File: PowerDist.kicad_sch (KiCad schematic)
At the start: 19 parts, among them U1 TPS2121RUXR

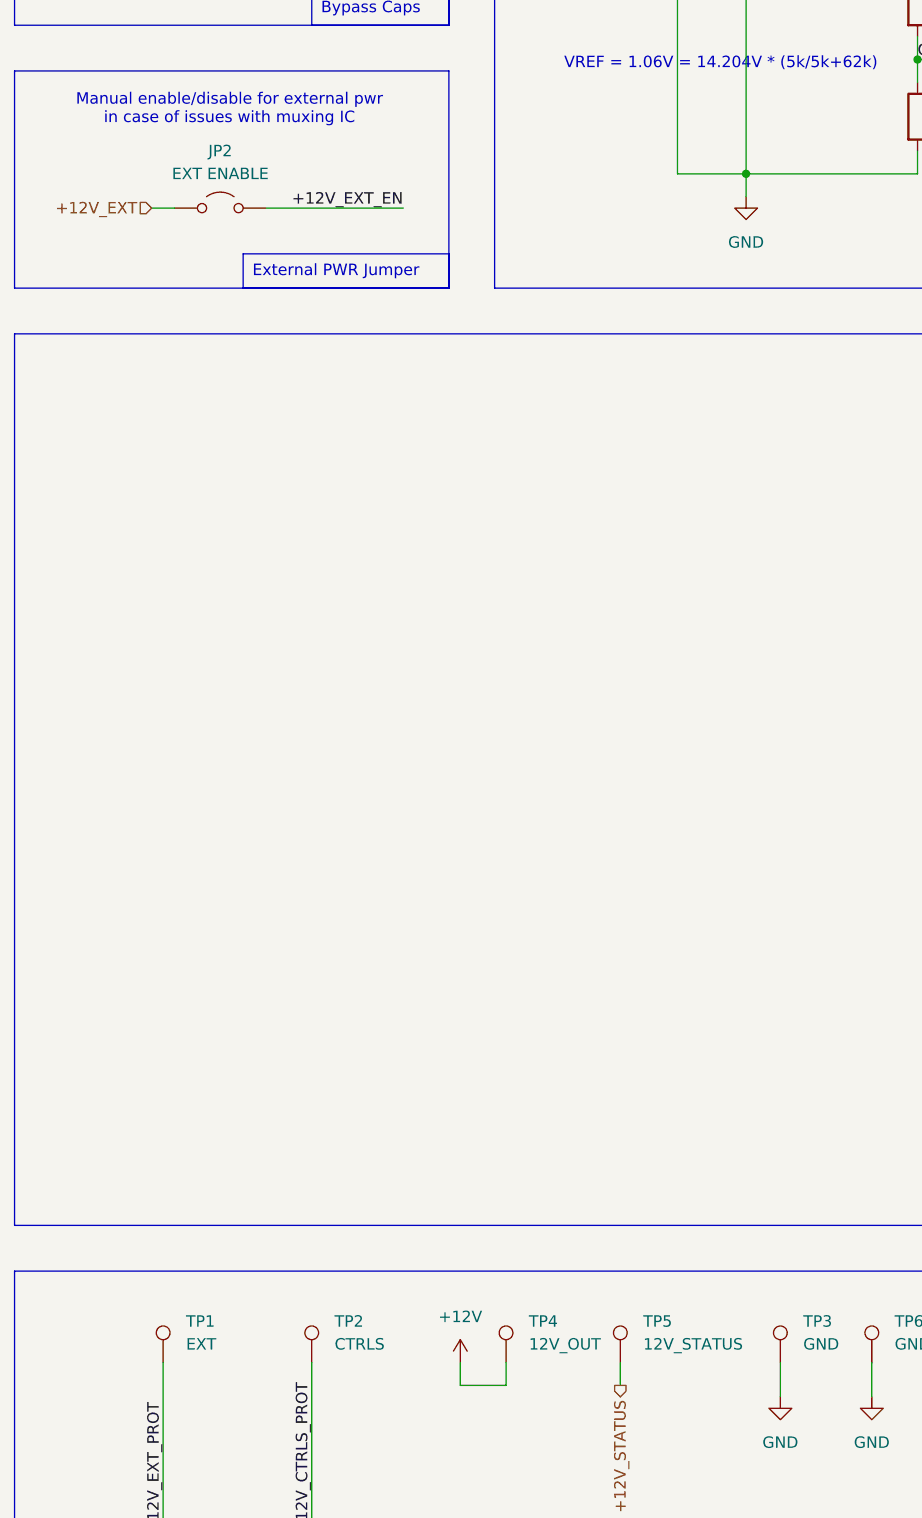
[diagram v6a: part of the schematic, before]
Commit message: flip connectors so clip faces inside
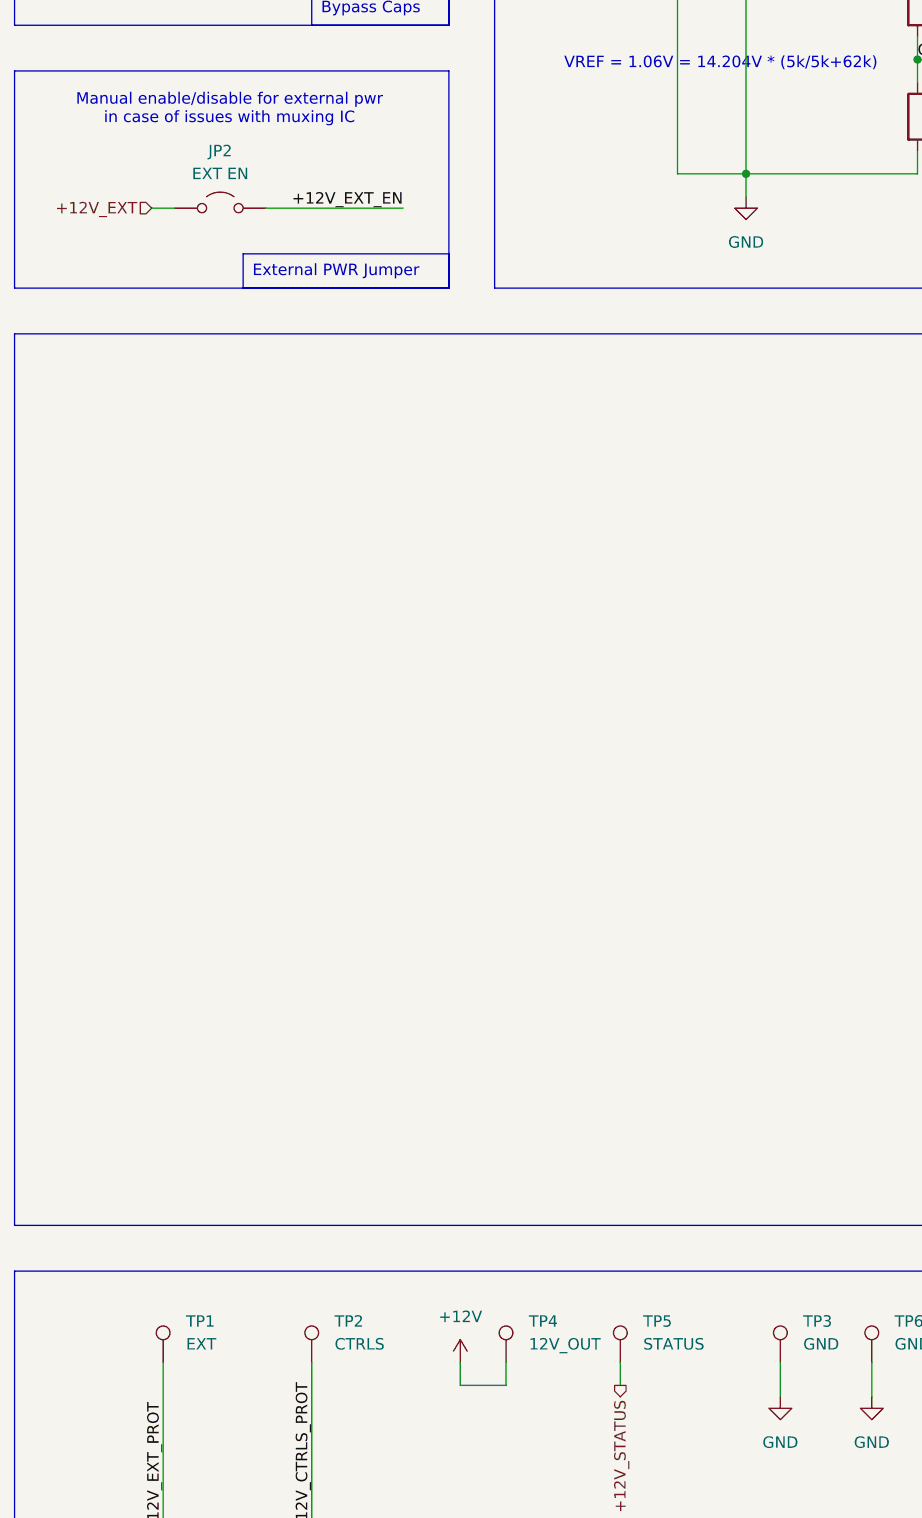
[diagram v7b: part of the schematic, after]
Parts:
- JP2: value EXT ENABLE -> EXT EN
- TP5: value 12V_STATUS -> STATUS
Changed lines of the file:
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@@
 			)
 		)
-		(property "Value" "12V_STATUS"
+		(property "Value" "STATUS"
 			(at 88.9 237.9979 0)
 			(effects
@@
 			)
 		)
-		(property "Value" "EXT ENABLE"
+		(property "Value" "EXT EN"
 			(at 41.91 107.95 0)
 			(effects

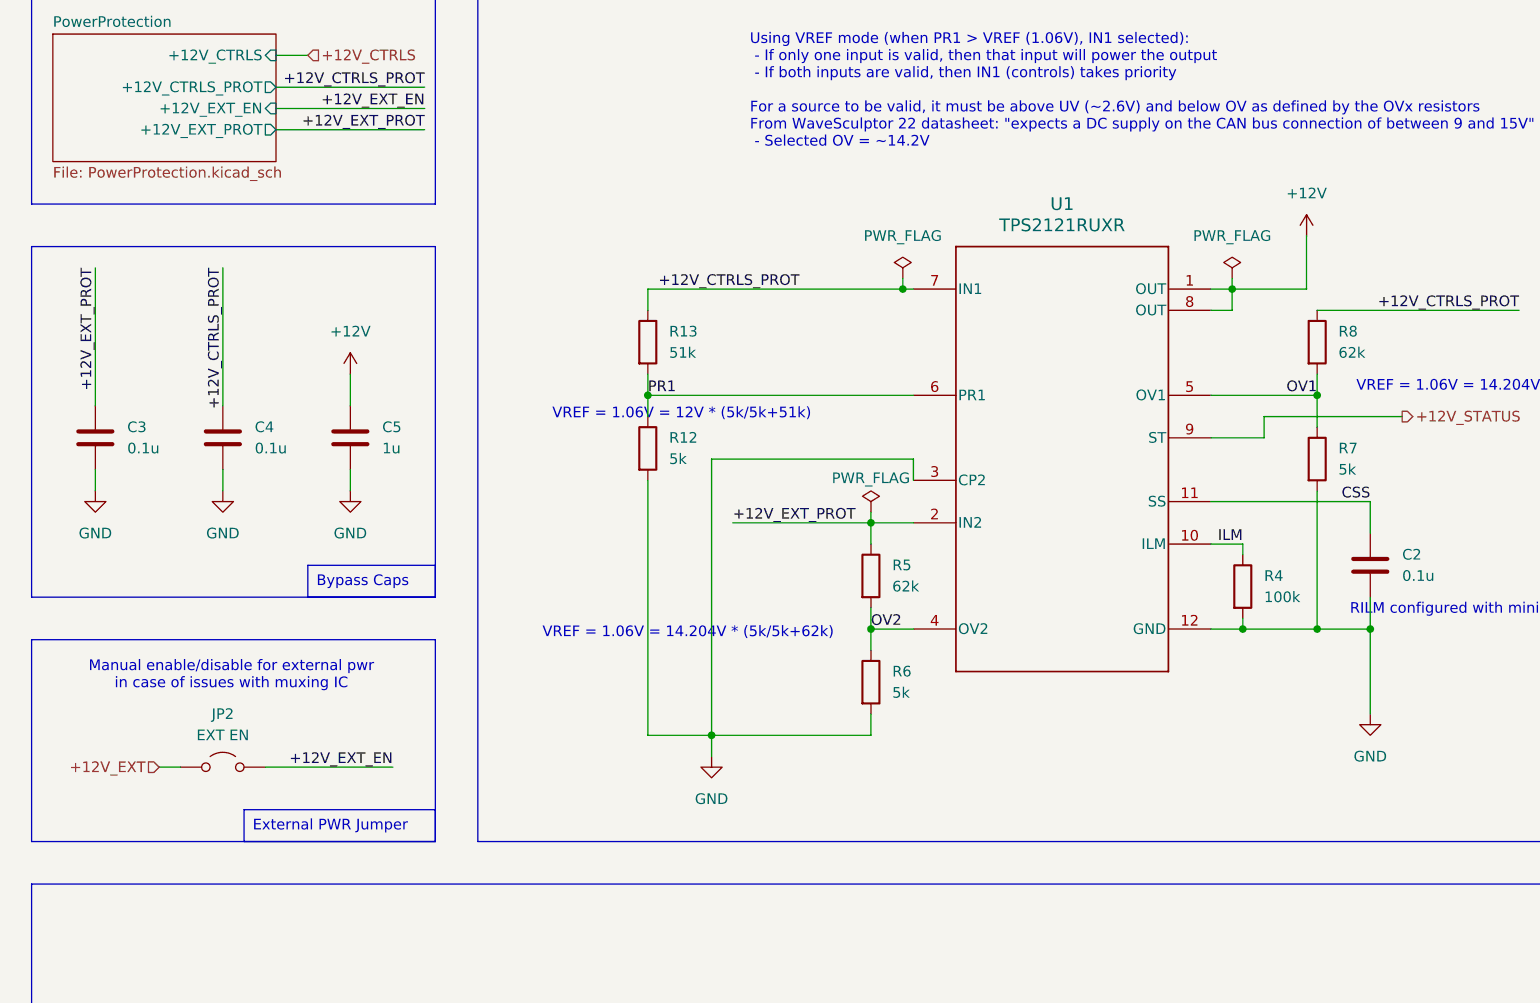
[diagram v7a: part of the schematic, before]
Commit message: output fuse and solder jumpers
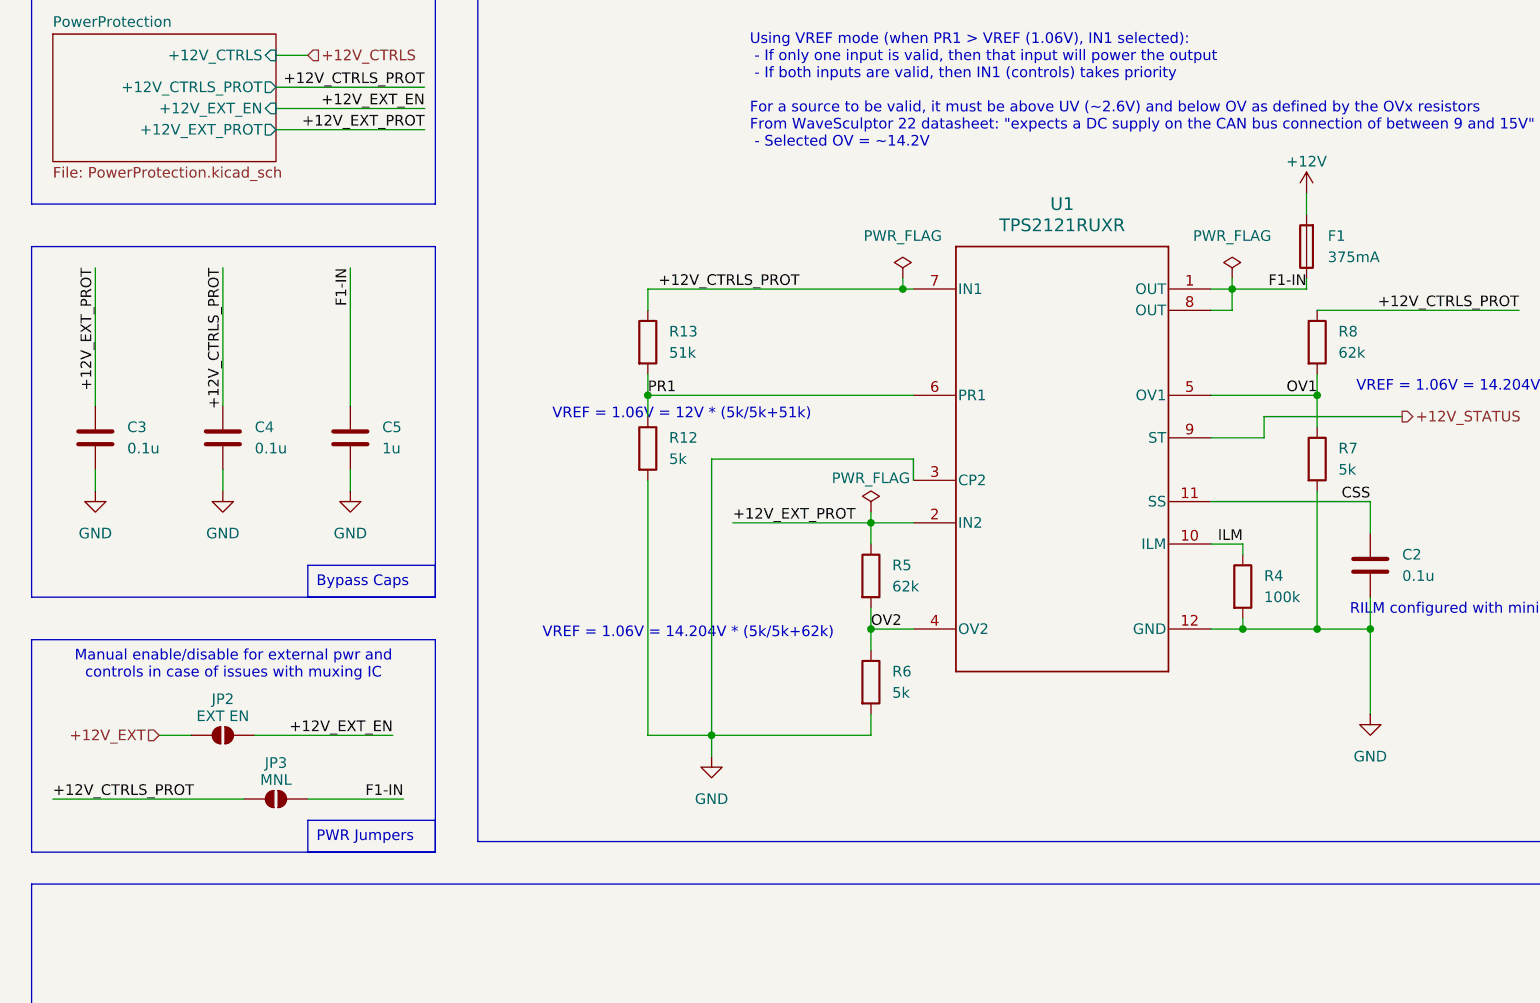
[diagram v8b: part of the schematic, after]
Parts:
- added F1: 375mA, Fuse:Fuse_1206_3216Metric, symbol Device:Fuse
- added JP3: MNL, Jumper:SolderJumper-2_P1.3mm_Open_RoundedPad1.0x1.5mm, symbol Jumper:SolderJumper_2_Open
- JP2: footprint Connector_PinHeader_2.54mm:PinHeader_1x02_P2.54mm_Vertical -> Jumper:SolderJumper-2_P1.3mm_Open_RoundedPad1.0x1.5mm; symbol Jumper:Jumper_2_Open -> Jumper:SolderJumper_2_Open; now left out of the parts list
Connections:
- net +12V: now also F1.2; no longer C5.1, U1.1 (OUT), U1.8 (OUT)
- net +12V_CTRLS_PROT: now also JP3.1 (A)
- new net F1-IN: C5.1, F1.1, JP3.2 (B), U1.1 (OUT), U1.8 (OUT)
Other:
- note added: "Manual enable/disable for external pwr and controls in case of issues with muxing IC"
- note removed: "Manual enable/disable for external pwr in case of issues with muxing IC"
